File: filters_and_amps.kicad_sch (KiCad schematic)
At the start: 29 parts, among them J2 Conn_02x02_Counter_Clockwise, J3 Conn_02x02_Counter_Clockwise, U4 LM833DT, U6 TL084IDT, U7 LM833DT

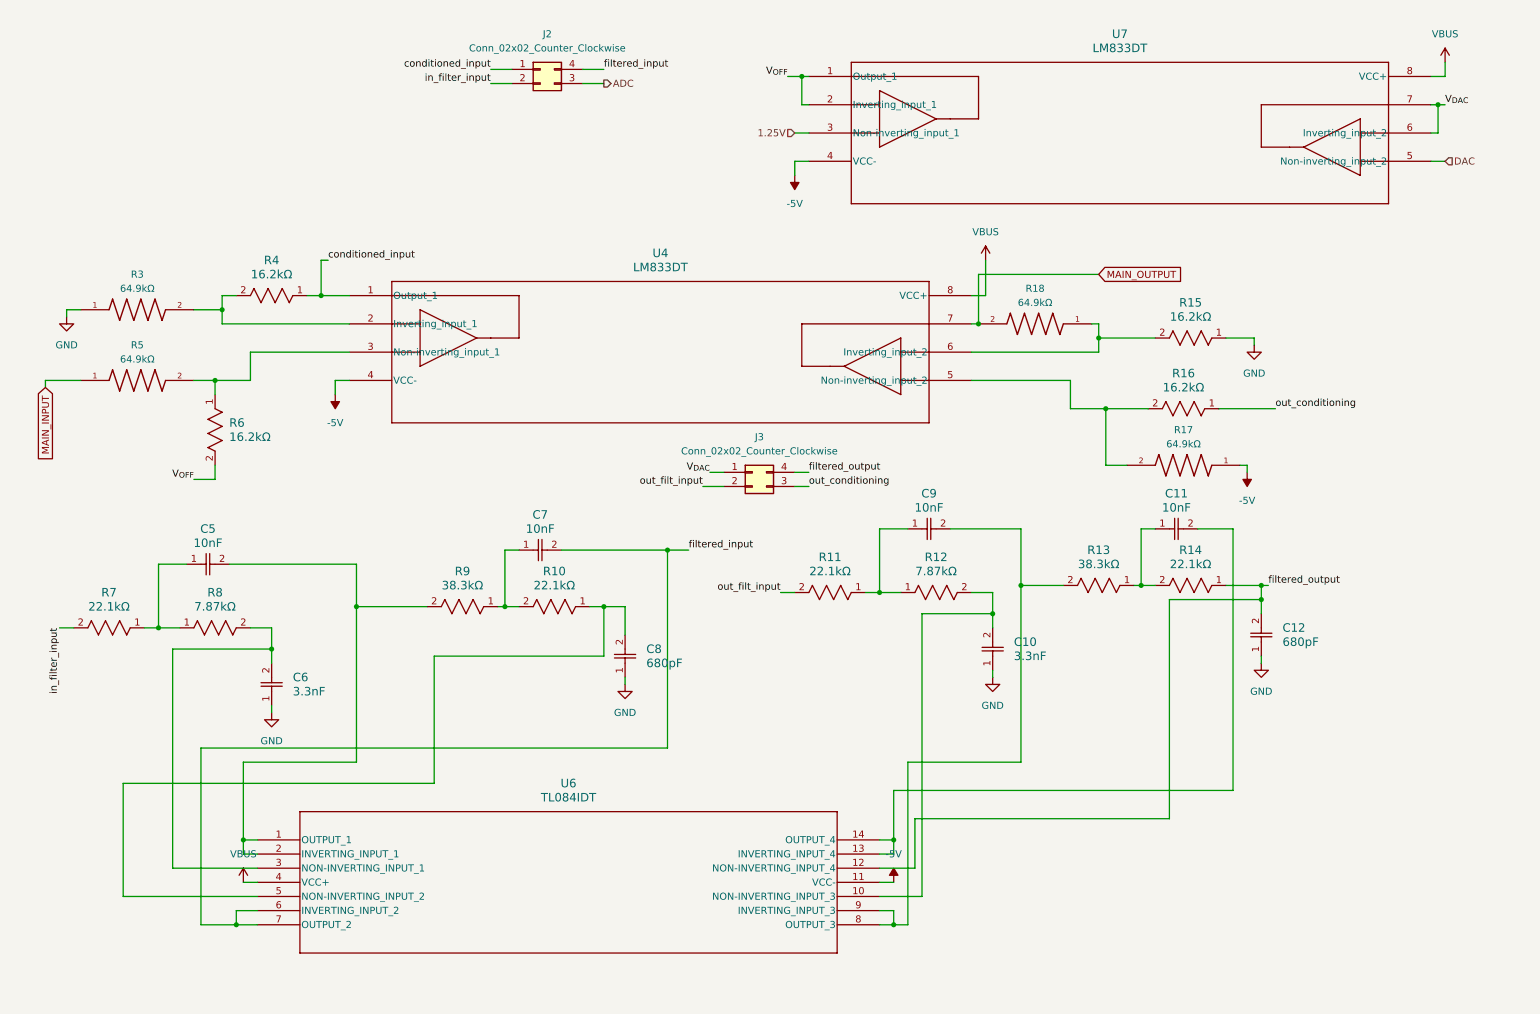
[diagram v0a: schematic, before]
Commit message: Finished the display and input switch schematics. Also added input buffers to the inputs and made them differential
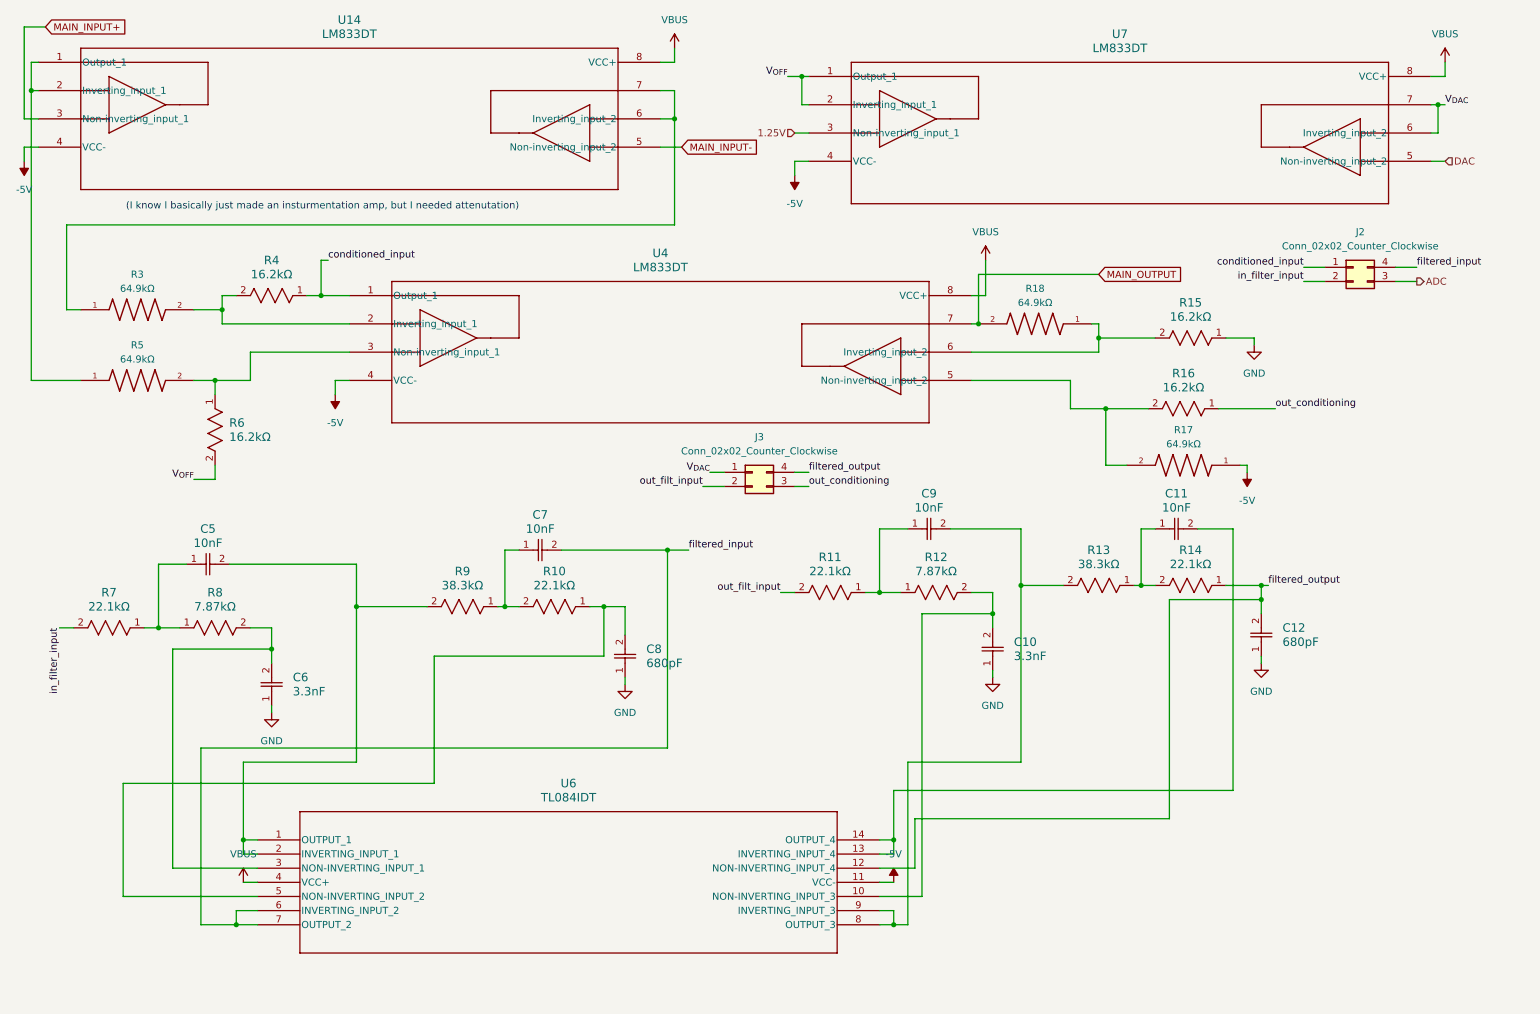
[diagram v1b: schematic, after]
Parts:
- added U14: LM833DT, SO_833DT_STM, symbol CMPE2750:LM833DT
- J2, J3: footprint (none) -> Connector_PinHeader_2.54mm:PinHeader_2x02_P2.54mm_Vertical
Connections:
- net -5V: now also U14.4 (VCC-)
- net GND: no longer R3.1
- net VBUS: now also U14.8 (VCC+)
- net MAIN_INPUT: no longer names the net of R5.1
- net MAIN_INPUT: now also U14.1 (Output_1), U14.2 (Inverting_input_1)
- new net: R3.1, U14.6 (Inverting_input_2), U14.7
- new net MAIN_INPUT+: U14.3 (Non-inverting_input_1)
- new net MAIN_INPUT-: U14.5 (Non-inverting_input_2)
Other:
- note added: "(I know I basically just made an insturmentation amp, but I needed attenutation)"
- moved on the sheet: J2

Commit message: Changed some parts so it now only uses one type of op amp
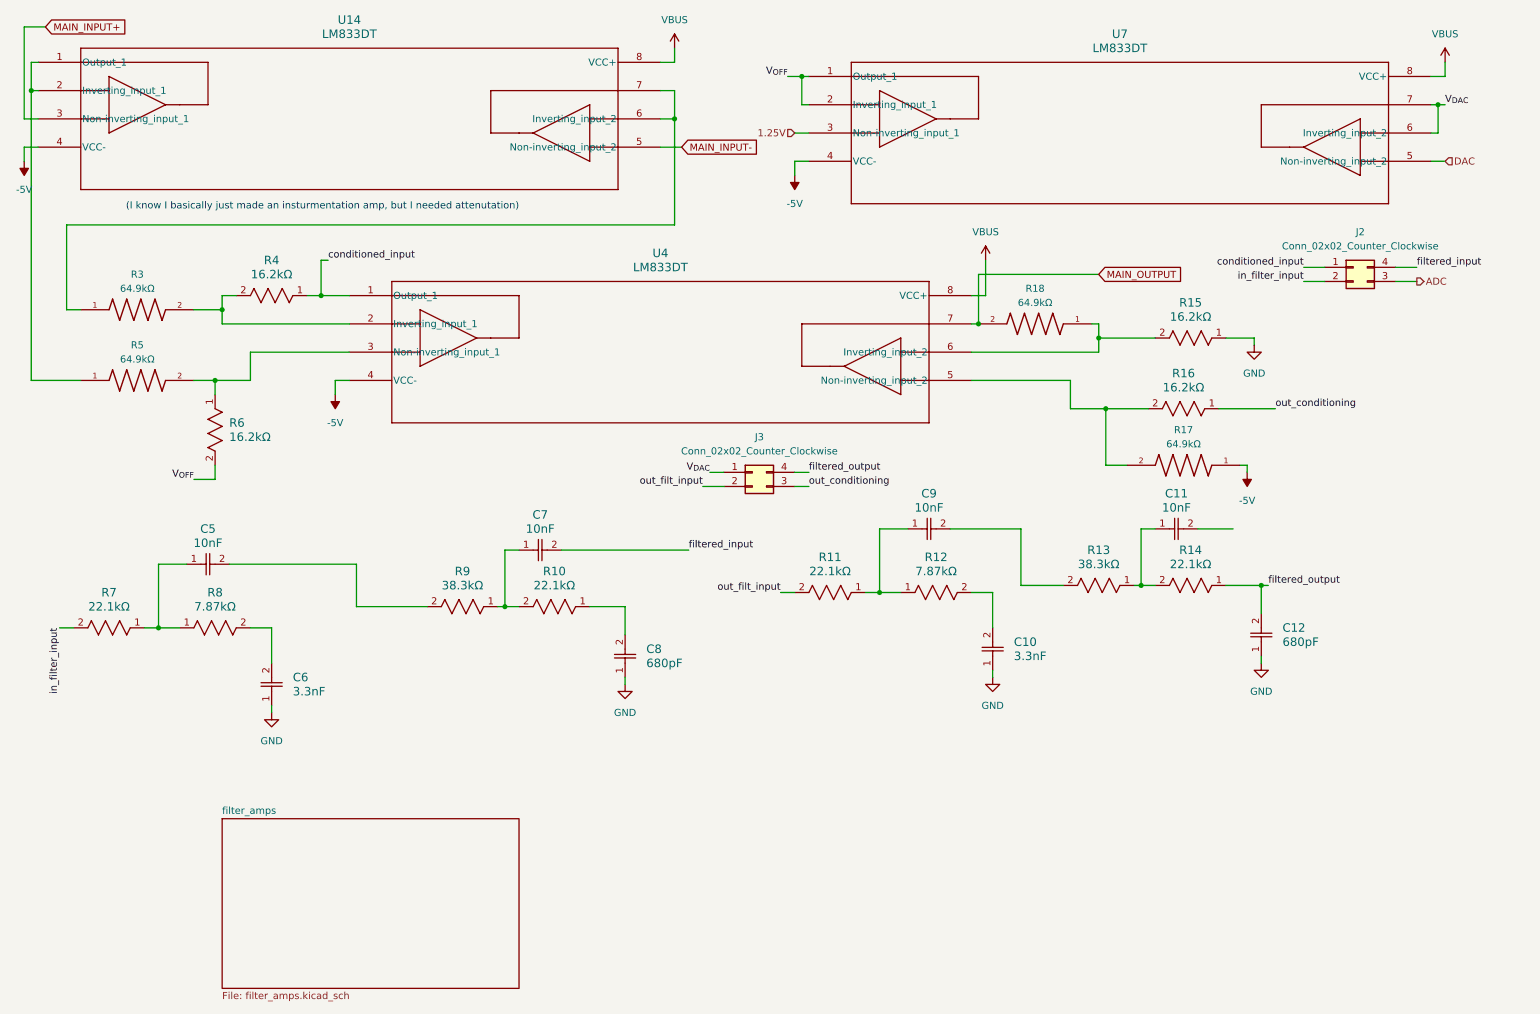
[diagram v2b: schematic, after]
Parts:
- removed U6: TL084IDT, SO14_TL084_STM, symbol CMPE2750:TL084IDT
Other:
- added sheet filter_amps (filter_amps.kicad_sch)

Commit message: Almost done. Just going to try and change something
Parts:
- added C15, C16, C17: 100nF, LMK212G_TAY, symbol CMPE2750:LMK212B7105KGHTR
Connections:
- net -5V: now also C15.2, C16.2, C17.2
- net VBUS: now also C15.1, C16.1, C17.1
- net Ooutput_2b: now reaches C11.2
- net Ooutput_2b: now also J3.4 (Pin_4)
- net V_{in-}: now reaches R3.1, U14.6 (Inverting_input_2), U14.7
- net Output_1a: now reaches C5.2, R9.2
- net Non-inverting_input_1b: now reaches C10.2, R12.2
- net Non-inverting_input_2a: now reaches C8.2, R10.1
- net Output_1b: now reaches C9.2, R13.2
- net Non-inverting_input_1a: now reaches C6.2, R8.2
- net MAIN_OUTPUT renamed OUT
- net filtered_input renamed Output_2a
- net filtered_output renamed Non-inverting_input_2b
- net Non-inverting_input_2b: no longer J3.4 (Pin_4)
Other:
- sheet filter_amps ports: added Inverting_input_1a, Inverting_input_1b, Inverting_input_2a, Inverting_input_2b, Non-inverting_input_1a, Non-inverting_input_1b, Non-inverting_input_2a, Non-inverting_input_2b, Ooutput_2b, Output_1a, Output_1b, Output_2a; removed none

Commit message: Schematic is done?
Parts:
- C11, C5, C7, C9: footprint CAP_CC1206_YAG -> Capacitor_SMD:C_0805_2012Metric; symbol CMPE2750:CC1206FKNPO8BN103 -> CMPE2750:GRM2195C1H103FA01D
- C12, C8: footprint CAP_CC1206_YAG -> Capacitor_SMD:C_1206_3216Metric
- C15, C16, C17: footprint LMK212G_TAY -> Capacitor_SMD:C_0402_1005Metric; symbol CMPE2750:LMK212B7105KGHTR -> CMPE2750:CL05B104KP5NNNC
- R10, R11, R14, R7: footprint RC0603N_YAG -> Resistor_SMD:R_0603_1608Metric
- R12, R15, R16, R4, R6, R8: footprint RC0402N_YAG -> Resistor_SMD:R_0402_1005Metric
- R13, R9: footprint RC0603N_YAG -> Resistor_SMD:R_0402_1005Metric; symbol CMPE2750:RT0603BRD0738K3L -> CMPE2750:0402WGF3832TCE
- R17, R18, R3, R5: value 64.9kΩ -> ERA2AEB6492X; footprint ERA2AEB6492X:RES_ERA2AEB6492X -> Resistor_SMD:R_0402_1005Metric
- U14, U4, U7: value LM833DT -> OPA1678IDR; footprint SO_833DT_STM -> Package_SO:SOIC-8_3.9x4.9mm_P1.27mm; symbol CMPE2750:LM833DT -> CMPE2750:OPA1678IDR
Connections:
- net Output_1a: now also R9.1; no longer R9.2
- net Output_1b: now also R13.1; no longer R13.2
- net at C11.1, R14.2: now also R13.2; no longer R13.1
- net at C7.1, R10.2: now also R9.2; no longer R9.1

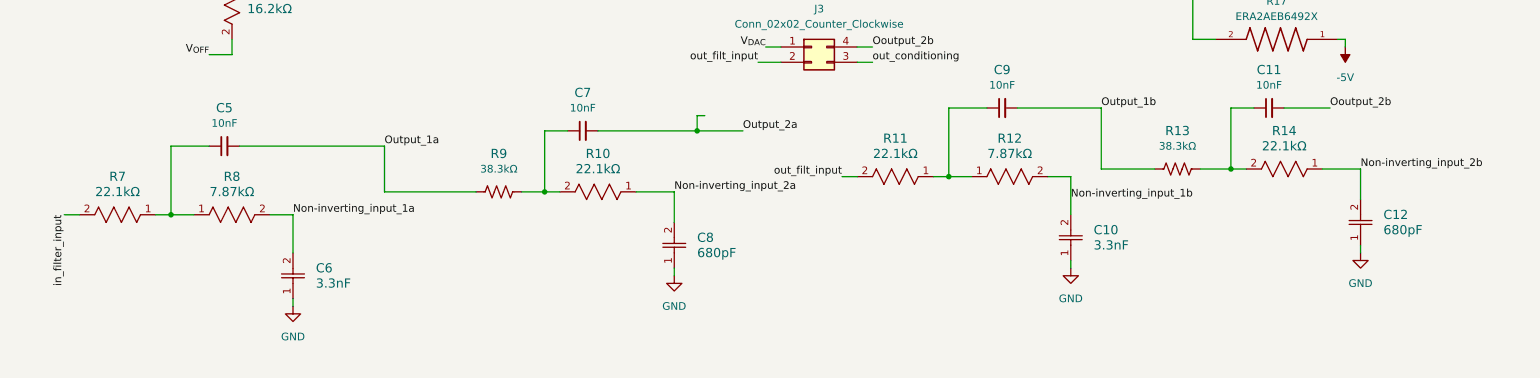
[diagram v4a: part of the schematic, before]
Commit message: Swapped the current limiting diodes for resistors. They *should* be good enough under normal operating conditions. Also added some pull-down resistors. Done?
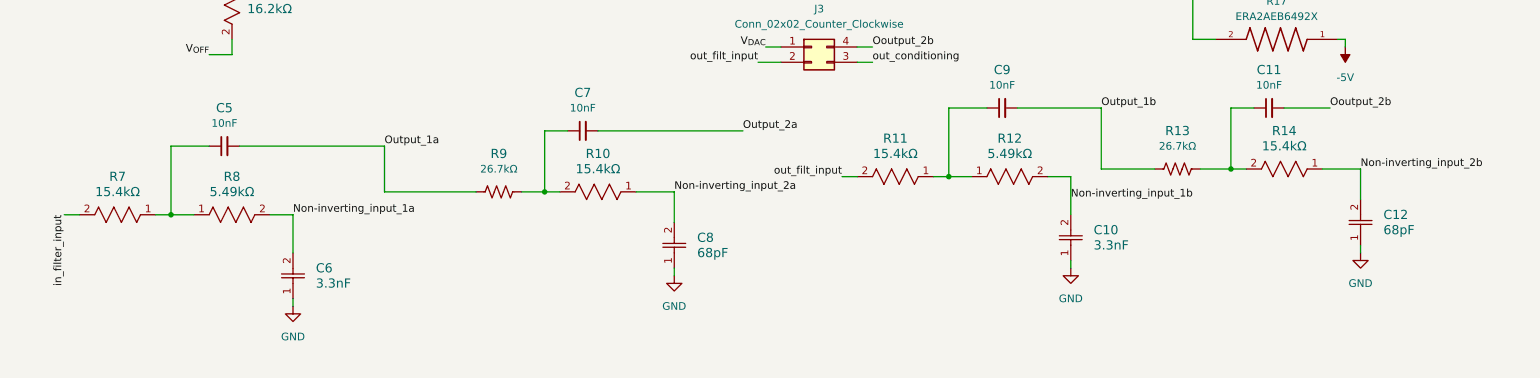
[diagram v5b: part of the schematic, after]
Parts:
- C12, C8: value 680pF -> 68pF; footprint Capacitor_SMD:C_1206_3216Metric -> Capacitor_SMD:C_0402_1005Metric
- R10, R11, R14, R7: value 22.1kΩ -> 15.4kΩ
- R12, R8: value 7.87kΩ -> 5.49kΩ
- R13, R9: value 38.3kΩ -> 26.7kΩ; footprint Resistor_SMD:R_0402_1005Metric -> Resistor_SMD:R_0603_1608Metric

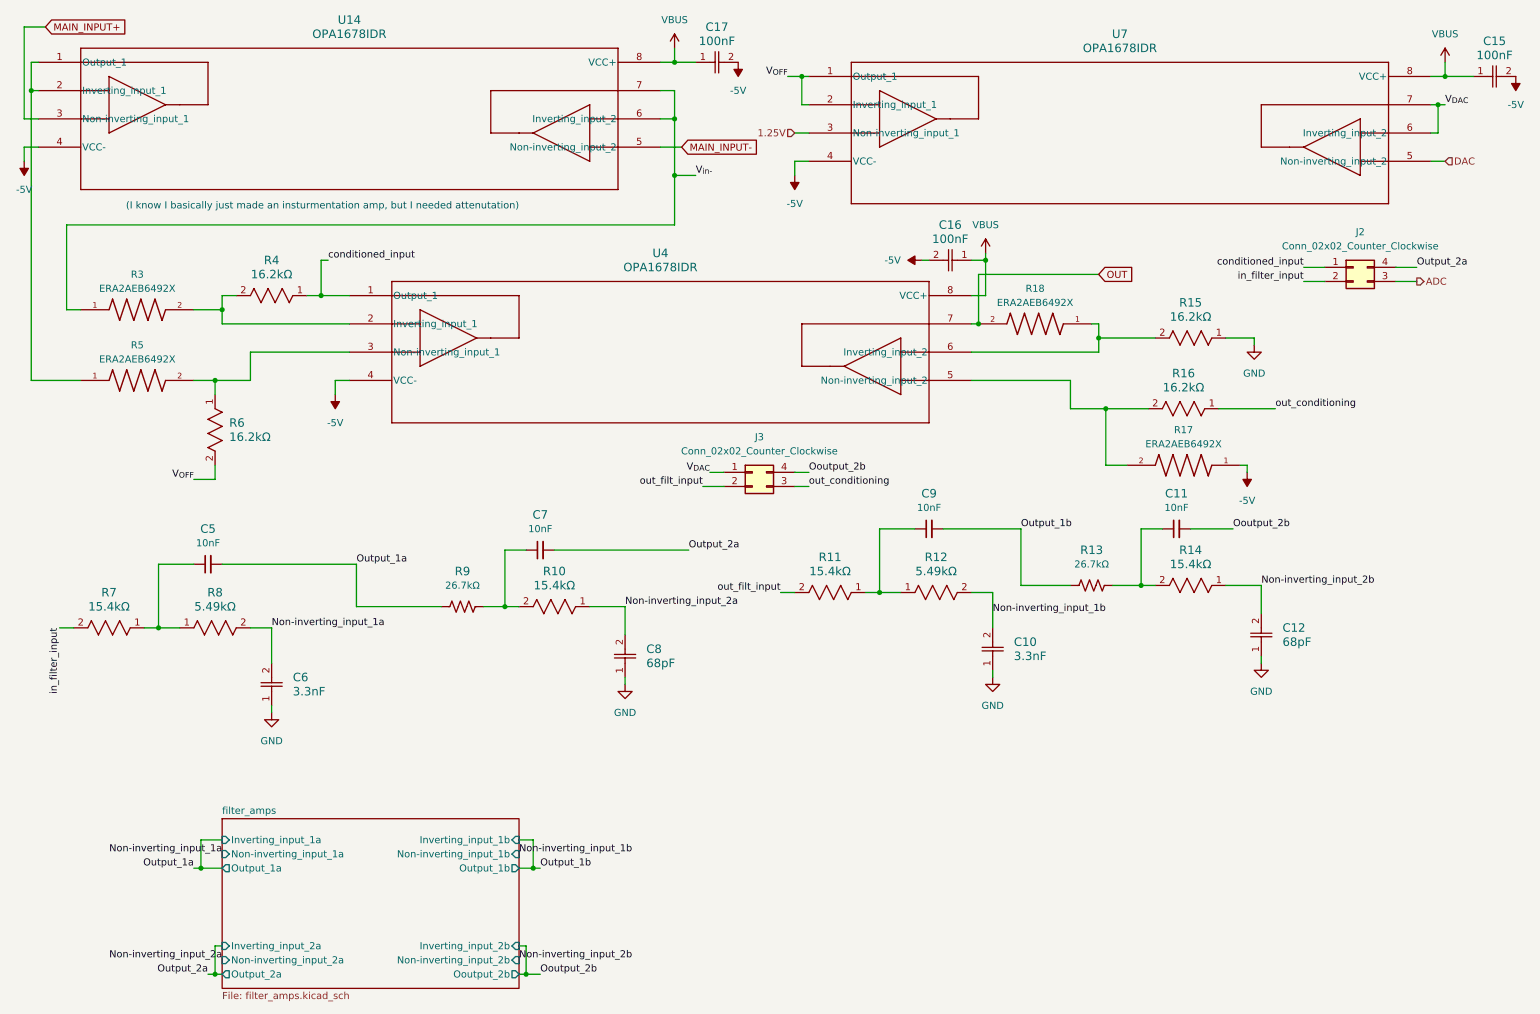
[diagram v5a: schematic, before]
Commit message: Added mounting holes to the schematic, reset the annotations, updated a few footprints, and fixed some issues that were discovered on the ERC.
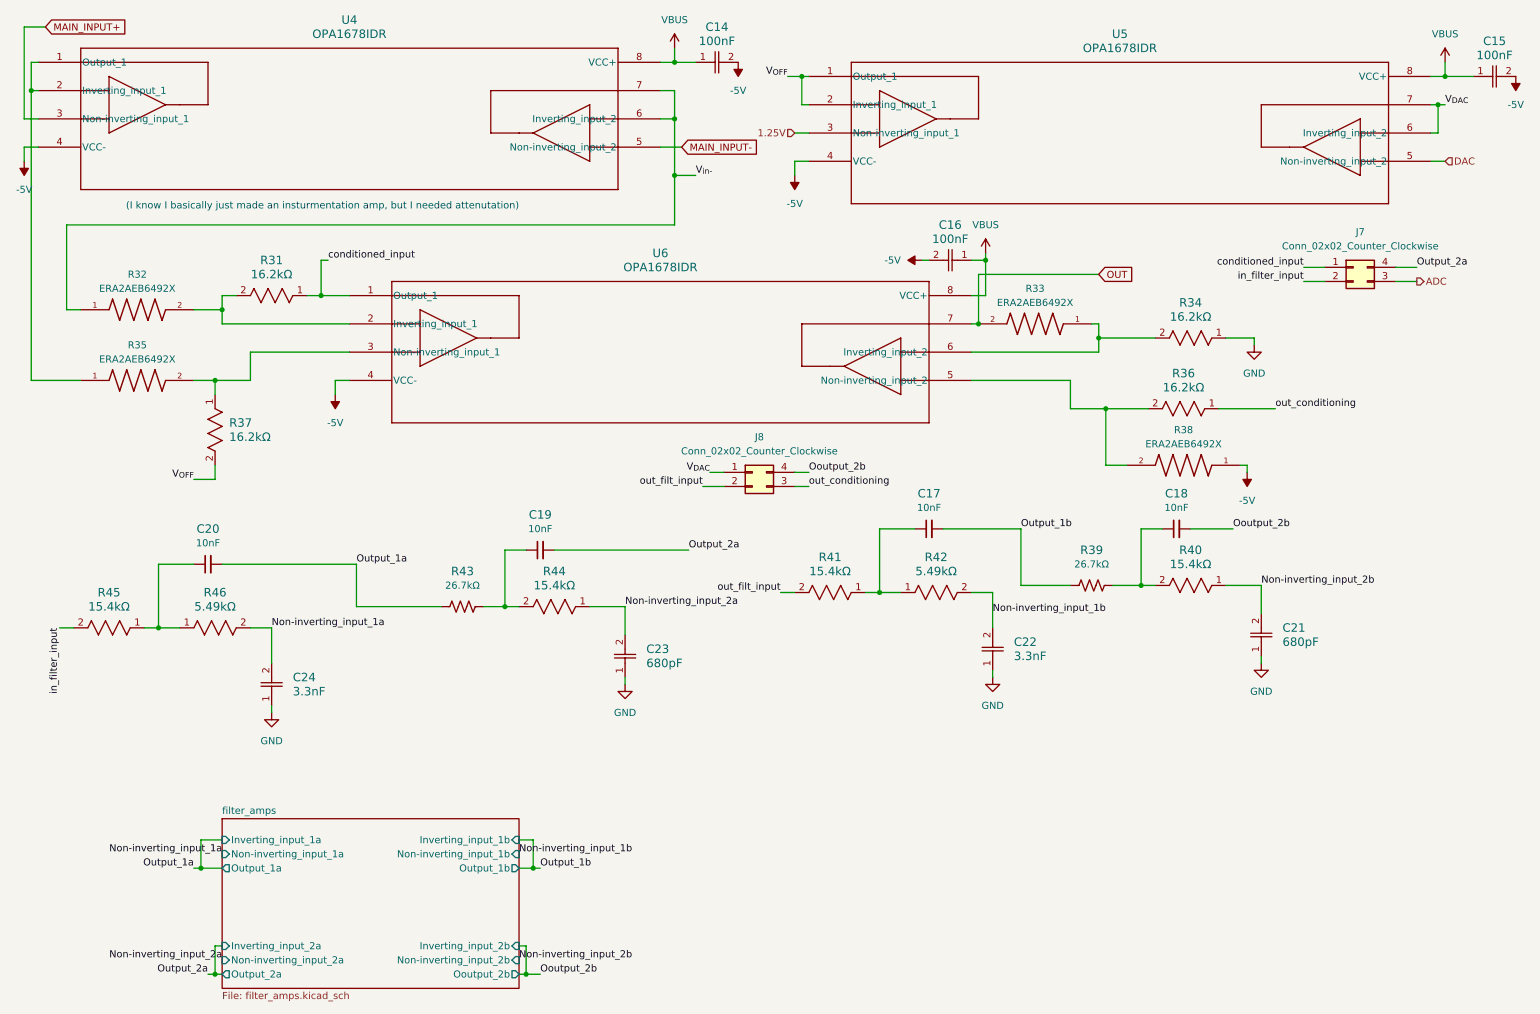
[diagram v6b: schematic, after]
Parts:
- C21: renamed from C12; value 68pF -> 680pF
- C22: renamed from C10; footprint Capacitor_SMD:C_1206_3216Metric -> Capacitor_SMD:C_0603_1608Metric
- C23: renamed from C8; value 68pF -> 680pF
- C24: renamed from C6; footprint Capacitor_SMD:C_1206_3216Metric -> Capacitor_SMD:C_0603_1608Metric
- renumbered C17 to C14, C9 to C17, C11 to C18, C7 to C19, C5 to C20, J2 to J7, J3 to J8, R4 to R31, R3 to R32, R18 to R33, R15 to R34, R5 to R35, R16 to R36, R6 to R37, R17 to R38, R13 to R39, R14 to R40, R11 to R41, R12 to R42, R9 to R43, R10 to R44, R7 to R45, R8 to R46, U14 to U4, U7 to U5, U4 to U6
